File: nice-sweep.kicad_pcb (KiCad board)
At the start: 2 copper layers, 222.8 x 89.6 mm, 88 parts, among them SW1 Kailh-Choc, SW10 Kailh-Choc, SW11 Kailh-Choc, SW12 Kailh-Choc, SW13 Kailh-Choc, SW14 Kailh-Choc, SW15 Kailh-Choc, SW16 Kailh-Choc, SW17 Kailh-Choc, SW18 Kailh-Choc, SW19 Kailh-Choc, SW2 Kailh-Choc, SW20 Kailh-Choc, SW21 Kailh-Choc, SW22 Kailh-Choc, SW23 Kailh-Choc, SW24 Kailh-Choc, SW25 Kailh-Choc, SW26 Kailh-Choc, SW27 Kailh-Choc, SW28 Kailh-Choc, SW29 Kailh-Choc, SW3 Kailh-Choc, SW30 Kailh-Choc, SW31 Kailh-Choc, SW32 Kailh-Choc, SW33 Kailh-Choc, SW34 Kailh-Choc, SW4 Kailh-Choc, SW5 Kailh-Choc, SW6 Kailh-Choc, SW7 Kailh-Choc, SW8 Kailh-Choc, SW9 Kailh-Choc, U1 nice_nano, U2 nice_nano

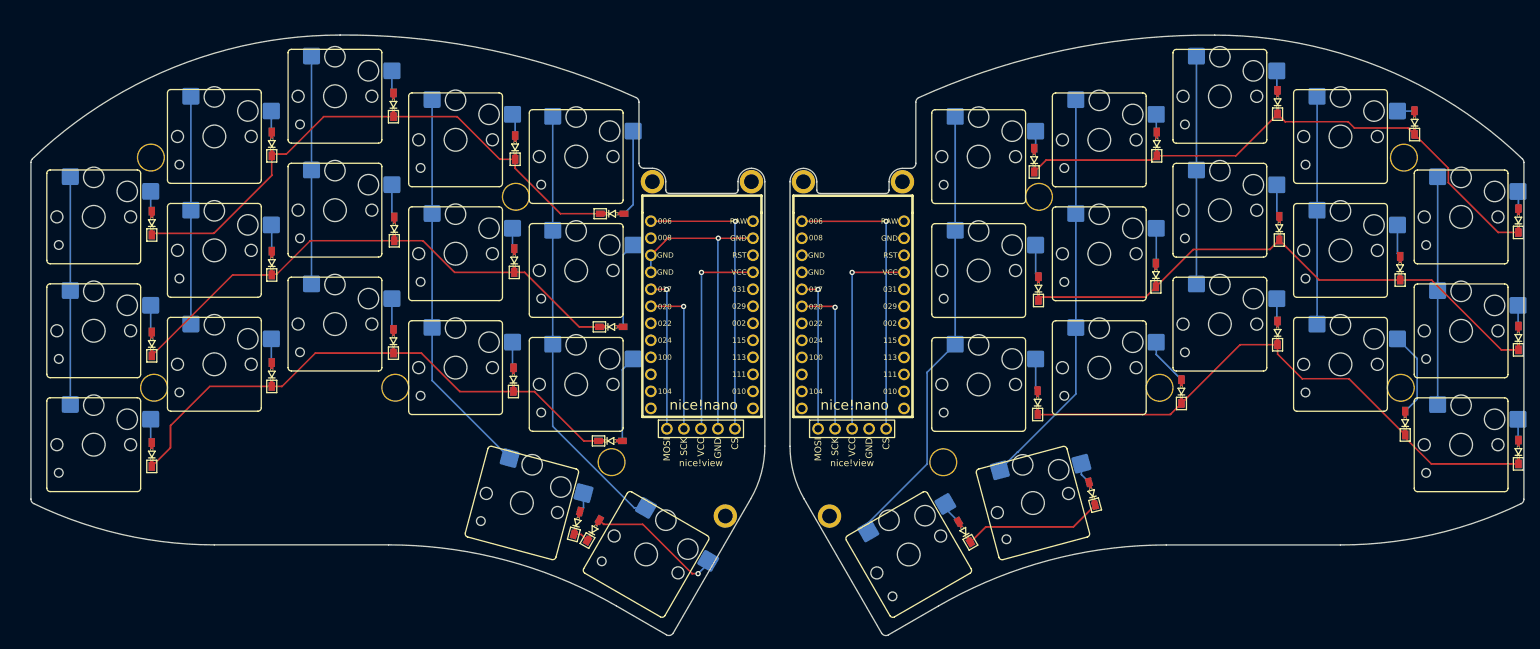
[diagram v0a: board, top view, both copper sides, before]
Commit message: Fix nice!nano orientation & add labels
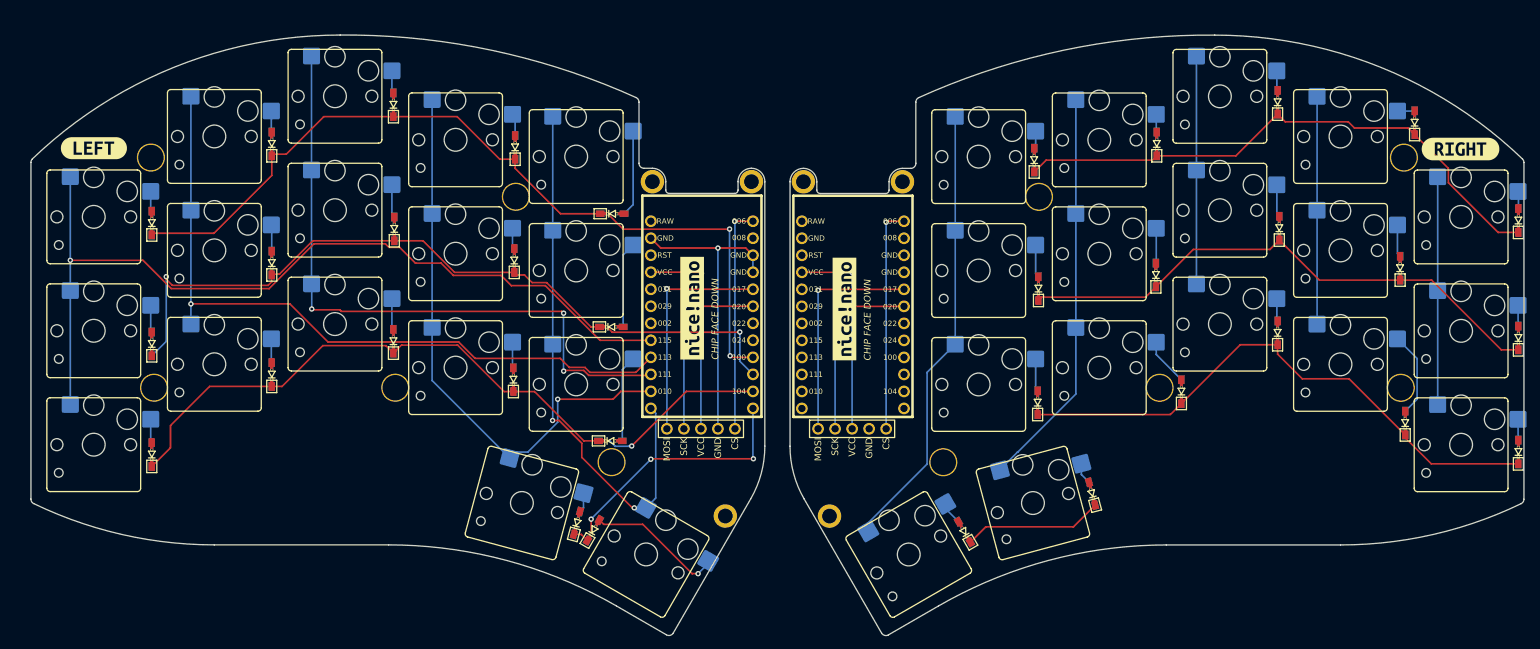
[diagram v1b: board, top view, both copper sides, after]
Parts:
- added kibuzzard-636136F9: G***, kibuzzard-636136F9, F.Cu at (29.6, 35.9)
- added kibuzzard-63613726: G***, kibuzzard-63613726, F.Cu at (233.6, 36.1)
- added kibuzzard-6361375E: G***, kibuzzard-6361375E, B.Cu at (65.4, 72.1)
- added kibuzzard-6361375E: G***, kibuzzard-6361375E, B.Cu at (200.5, 72.5)
- added kibuzzard-6361381D: G***, kibuzzard-6361381D, F.Cu at (118.9, 59.8)
- added kibuzzard-6361381D: G***, kibuzzard-6361381D, F.Cu at (141.6, 59.9)
- U1, U2: moved to B.Cu
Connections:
- U1 pad 10: unconnected-(U1-Pad10) -> ROW1
- U1 pad 11: unconnected-(U1-Pad11) -> ROW2
- U1 pad 12: unconnected-(U1-Pad12) -> ROW3
- U1 pad 13: unconnected-(U1-Pad13) -> COL4
- U1 pad 14: unconnected-(U1-Pad14) -> COL3
- U1 pad 15: unconnected-(U1-Pad15) -> COL2
- U1 pad 16: unconnected-(U1-Pad16) -> COL1
- U1 pad 17: unconnected-(U1-Pad17) -> COL0
- U1 pad 9: unconnected-(U1-Pad9) -> ROW0
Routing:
- net COL0: track 34.0 -> 131.1 mm, vias 0 -> 1
- net COL1: track 34.0 -> 107.8 mm, vias 0 -> 1
- net COL2: track 34.0 -> 97.7 mm, vias 0 -> 3
- net ROW0: track 82.8 -> 124.4 mm, vias 0 -> 2
- net ROW3: track 2.41 -> 40.2 mm, vias 0 -> 3
- net ROW1: track 79.2 -> 114.1 mm, vias 0 -> 2
- net ROW2: track 81.0 -> 108.6 mm, vias 0 -> 1
- net COL3: track 58.3 -> 85.5 mm, vias 0 -> 1
- net COL4: track 65.2 -> 81.7 mm, vias 0 -> 2
- net MOSI: track 23.2 -> 33.9 mm
- net R_MOSI: track 23.2 -> 33.6 mm
- net R_NVCS: track 43.5 -> 33.6 mm
- net NVCS: track 43.6 -> 33.7 mm
- net SCK: track 23.2 -> 28.5 mm
- net R_SCK: track 23.1 -> 28.5 mm
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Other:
- board text added: "CHIP FACE DOWN"

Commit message: Update PCB with missing components
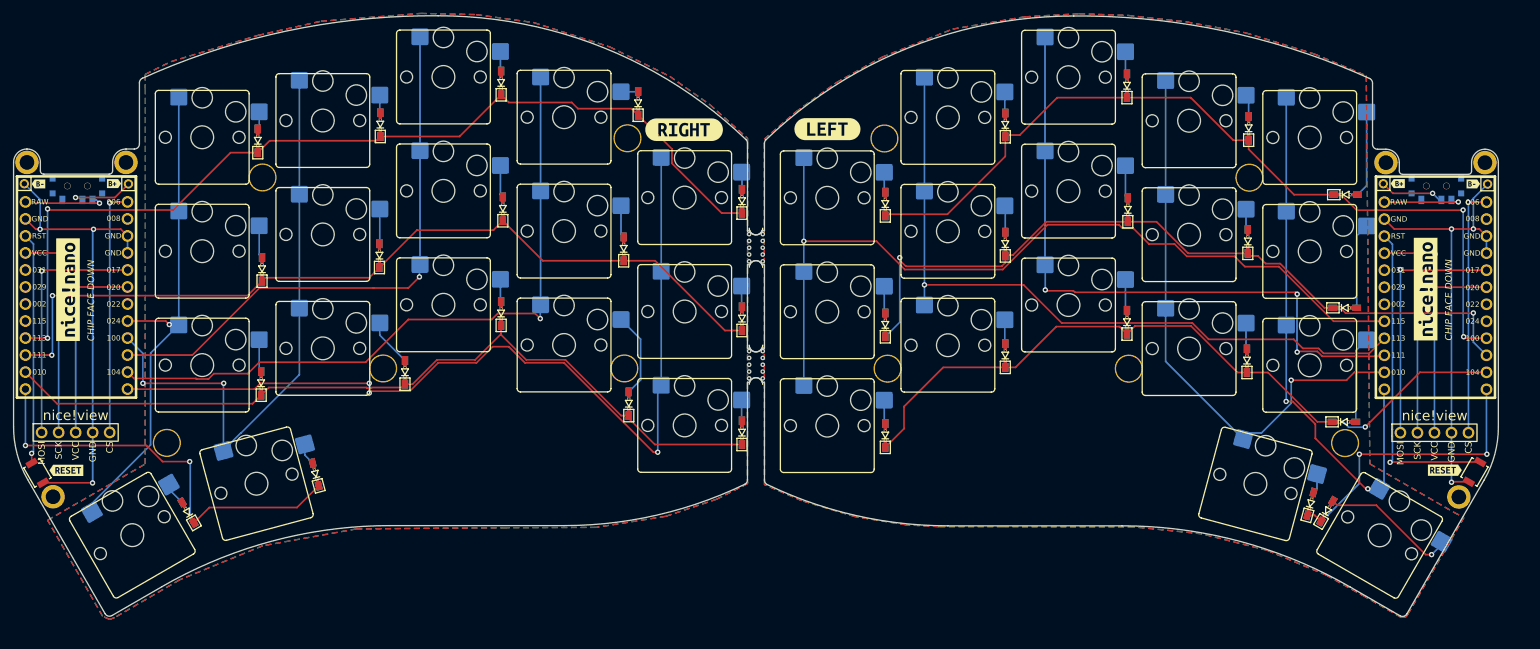
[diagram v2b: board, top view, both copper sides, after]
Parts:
- added Bat+0: MountingHole_Pad, * duckyb-collection:1pin_conn, F.Cu at (222.0, 41.2)
- added Bat+1: MountingHole_Pad, * duckyb-collection:1pin_conn, F.Cu at (34.7, 41.3)
- added BatGND0: MountingHole_Pad, * duckyb-collection:1pin_conn, F.Cu at (237.6, 41.3)
- added BatGND1: MountingHole_Pad, * duckyb-collection:1pin_conn, F.Cu at (19.2, 41.2)
- added RSW0: SW_Push, * duckyb-collection:SW_RESET, F.Cu at (235.6, 84.3)
- added RSW1: SW_Push, * duckyb-collection:SW_RESET, F.Cu at (21.2, 84.4)
- added SW_POWER0: SW_SPDT, * duckyb-collection:SPDT_C128955, B.Cu at (229.9, 41.6)
- added SW_POWER1: SW_SPDT, * duckyb-collection:SPDT_C128955, B.Cu at (27.1, 41.6)
- added kibuzzard-6361AD03: G***, kibuzzard-6361AD03, F.Cu at (32.6, 41.2)
- added kibuzzard-6361AD03: G***, kibuzzard-6361AD03, B.Cu at (224.2, 41.2)
- added kibuzzard-6361AD3F: G***, kibuzzard-6361AD3F, F.Cu at (21.3, 41.3)
- added kibuzzard-6361AD3F: G***, kibuzzard-6361AD3F, B.Cu at (235.5, 41.3)
- added kibuzzard-6361AD8B: G***, kibuzzard-6361AD8B, F.Cu at (235.5, 41.3)
- added kibuzzard-6361AD8B: G***, kibuzzard-6361AD8B, B.Cu at (21.3, 41.3)
- added kibuzzard-6361ADA3: G***, kibuzzard-6361ADA3, F.Cu at (224.2, 41.2)
- added kibuzzard-6361ADA3: G***, kibuzzard-6361ADA3, B.Cu at (32.6, 41.2)
- added kibuzzard-6361B5A3: G***, kibuzzard-6361B5A3, F.Cu at (231.2, 84.0)
- added kibuzzard-6361B5B5: G***, kibuzzard-6361B5B5, F.Cu at (25.5, 84.0)
- added mouse-bite-2mm-slot: VAL**, Duckyb-Parts:mouse-bite-5mm-slot-with-space-for-track, F.Cu at (128.4, 50.8)
- added mouse-bite-2mm-slot: VAL**, Duckyb-Parts:mouse-bite-5mm-slot-with-space-for-track, F.Cu at (128.4, 68.3)
- moved D25 115.9 mm to (90.6, 45.0)
- moved SW34 115.9 mm to (53.9, 86.0)
- moved D19 115.9 mm to (72.3, 32.4)
- moved D23 115.9 mm to (54.7, 54.0)
- moved D26 115.9 mm to (108.7, 51.0)
- moved D28 115.9 mm to (54.6, 71.0)
- moved D31 115.9 mm to (109.4, 74.1)
- moved D33 115.9 mm to (43.6, 90.3)
- moved D34 115.9 mm to (62.7, 84.6)
- moved H1 115.9 mm to (109.2, 34.5)
- moved H2 115.9 mm to (108.8, 68.8)
- moved H3 115.9 mm to (54.8, 40.3)
- moved H4 115.9 mm to (40.5, 79.9)
- moved H4 115.9 mm to (72.8, 68.8)
- moved Ref** 115.9 mm to (34.4, 38.1)
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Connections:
- U1 pad 22: unconnected-(U1-Pad22) -> RESET
- U1 pad 24: unconnected-(U1-Pad24) -> RAW
- U2 pad 10: unconnected-(U2-Pad10) -> R_COL2
- U2 pad 11: unconnected-(U2-Pad11) -> R_COL3
- U2 pad 12: unconnected-(U2-Pad12) -> R_COL4
- U2 pad 13: unconnected-(U2-Pad13) -> R_ROW3
- U2 pad 14: unconnected-(U2-Pad14) -> R_ROW2
- U2 pad 15: unconnected-(U2-Pad15) -> R_ROW1
- U2 pad 16: unconnected-(U2-Pad16) -> R_ROW0
- U2 pad 22: unconnected-(U2-Pad22) -> R_RESET
- U2 pad 23: unconnected-(U2-Pad23) -> R_GND
- U2 pad 24: unconnected-(U2-Pad24) -> R_RAW
- U2 pad 3: unconnected-(U2-Pad3) -> R_GND
- U2 pad 4: unconnected-(U2-Pad4) -> R_GND
- U2 pad 8: unconnected-(U2-Pad8) -> R_COL0
- U2 pad 9: unconnected-(U2-Pad9) -> R_COL1
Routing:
- net R_COL4: track 34.0 -> 134.5 mm, vias 0 -> 3
- net R_GND: track 0.00 -> 71.9 mm, vias 0 -> 3
- net R_COL3: track 34.0 -> 102.5 mm, vias 0 -> 1
- net R_ROW0: track 84.4 -> 142.0 mm, vias 0 -> 2
- net R_COL2: track 34.0 -> 84.3 mm, vias 0 -> 1
- net RESET: track 0.00 -> 47.9 mm, vias 0 -> 1
- net R_ROW1: track 82.1 -> 127.2 mm, vias 0 -> 2
- net R_ROW3: track 20.9 -> 63.1 mm, vias 0 -> 2
- net R_ROW2: track 84.5 -> 123.0 mm
- net R_RESET: track 0.00 -> 34.5 mm, vias 0 -> 1
- net R_COL1: track 60.0 -> 89.9 mm, vias 0 -> 2
- net GND: track 45.8 -> 66.8 mm, vias 1 -> 3
- net R_RAW: track 0.00 -> 12.4 mm, vias 0 -> 1
- net RAW: track 0.00 -> 12.2 mm, vias 0 -> 1
- net R_BT+: track 0.00 -> 9.91 mm, vias 0 -> 1
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- added copper zone on B.Cu, net (none)
- added copper zone on F.Cu, net (none)
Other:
- board size 222.8 x 89.6 mm -> 221.6 x 89.6 mm
- board text added: "nice!view"

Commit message: Update silkscreens
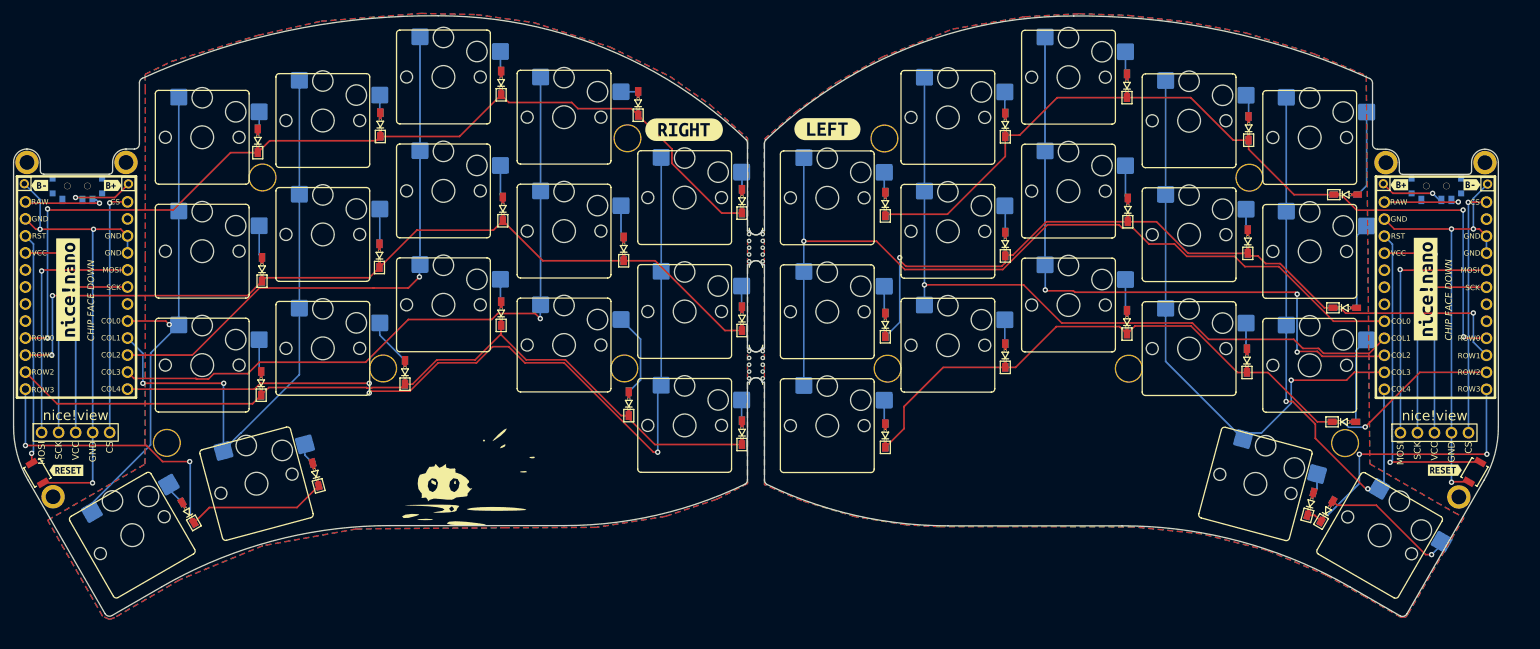
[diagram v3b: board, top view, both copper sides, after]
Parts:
- removed kibuzzard-6361AD03 (x2): G***, kibuzzard-6361AD03
- removed kibuzzard-6361AD3F (x2): G***, kibuzzard-6361AD3F
- removed kibuzzard-6361AD8B (x2): G***, kibuzzard-6361AD8B
- removed kibuzzard-6361ADA3 (x2): G***, kibuzzard-6361ADA3
- added G***: LOGO, LOGO, F.Cu at (83.7, 83.7)
- added G***: LOGO, LOGO, F.Cu at (83.9, 81.5)
- added REF**: OSHW-Symbol_6.7x6mm_SilkScreen, Symbol:OSHW-Symbol_6.7x6mm_SilkScreen, B.Cu at (87.2, 80.9)
- added kibuzzard-6361BA49: G***, kibuzzard-6361BA49, B.Cu at (87.2, 85.8)
- added kibuzzard-6361C7AA: G***, kibuzzard-6361C7AA, B.Cu at (86.7, 88.2)
- added kibuzzard-6361C84E: G***, kibuzzard-6361C84E, B.Cu at (230.0, 45.6)
- added kibuzzard-6361C84E: G***, kibuzzard-6361C84E, B.Cu at (26.9, 45.5)
- added kibuzzard-6361C879: G***, kibuzzard-6361C879, F.Cu at (224.4, 41.4)
- added kibuzzard-6361C891: G***, kibuzzard-6361C891, B.Cu at (224.4, 41.4)
- added kibuzzard-6361C8A5: G***, kibuzzard-6361C8A5, F.Cu at (235.3, 41.4)
- added kibuzzard-6361C8CA: G***, kibuzzard-6361C8CA, B.Cu at (235.3, 41.4)
- added kibuzzard-6361C962: G***, kibuzzard-6361C962, F.Cu at (32.4, 41.5)
- added kibuzzard-6361C975: G***, kibuzzard-6361C975, B.Cu at (32.4, 41.5)
- added kibuzzard-6361C99D: G***, kibuzzard-6361C99D, F.Cu at (21.5, 41.5)
- added kibuzzard-6361C9A3: G***, kibuzzard-6361C9A3, B.Cu at (21.5, 41.5)
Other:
- board text added: "COL2"
- board text added: "COL4"
- board text added: "CS"
- board text added: "GND"
- board text added: "MOSI"
- board text added: "ROW1"
- board text added: "ROW3"
- board text added: "SCK"
- board text added: "VCC"
